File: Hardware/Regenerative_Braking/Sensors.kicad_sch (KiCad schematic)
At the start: 48 parts, among them IC4 LM339DT

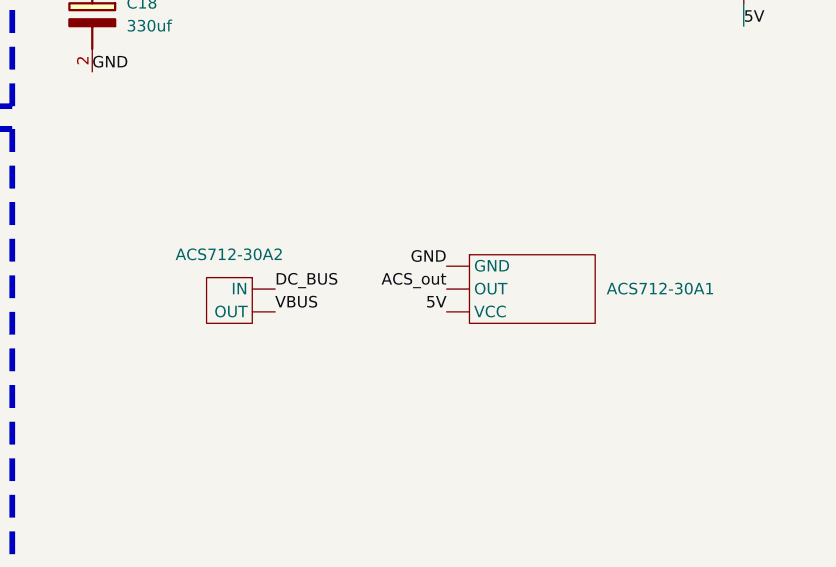
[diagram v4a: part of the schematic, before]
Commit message: Added Battery side
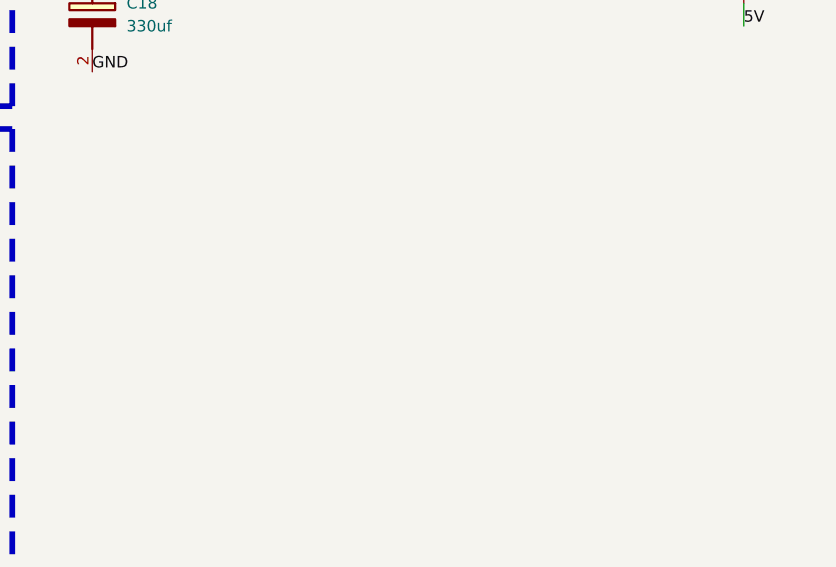
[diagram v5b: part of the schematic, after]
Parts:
- removed ACS712-30A1: (no value), Regen_braking:ACS712_Module_27x12mm, symbol Regen_braking:ACS712-30A
- removed ACS712-30A2: (no value), Regen_braking:Solderpad_acs712_INOUT, symbol Regen_braking:solder_pad_acs712_inout
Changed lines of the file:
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@@
 		)
 	)
-	(label "ACS_out"
-		(at 241.3 78.74 180)
-		(effects
-			(font
-				(size 1.27 1.27)
-			)
-			(justify right bottom)
-		)
-	)
 	(label "3V3"
 		(at 160.02 77.47 90)
@@
 	)
 	(label "VBUS"
-		(at 222.25 81.28 0)
-		(effects
-			(font
-				(size 1.27 1.27)
-			)
-			(justify left bottom)
-		)
-	)
-	(label "VBUS"
 		(at 27.94 161.29 180)
 		(effects
@@
 		)
 	)
-	(label "DC_BUS"
-		(at 222.25 78.74 0)
-		(effects
-			(font
-				(size 1.27 1.27)
-			)
-			(justify left bottom)
-		)
-	)
 	(label "3V3"
 		(at 81.28 102.87 0)
@@
 	)
 	(label "GND"
-		(at 241.3 76.2 180)
-		(effects
-			(font
-				(size 1.27 1.27)
-			)
-			(justify right bottom)
-		)
-	)
-	(label "GND"
 		(at 262.89 36.83 0)
 		(effects
@@
 		)
 	)
-	(label "5V"
-		(at 241.3 81.28 180)
-		(effects
-			(font
-				(size 1.27 1.27)
-			)
-			(justify right bottom)
-		)
-	)
 	(label "3V3"
 		(at 120.65 77.47 90)
@@
 	)
 	(symbol
-		(lib_id "Regen_braking:ACS712-30A")
-		(at 250.19 78.74 0)
-		(unit 1)
-		(body_style 1)
-		(exclude_from_sim no)
-		(in_bom yes)
-		(on_board yes)
-		(in_pos_files yes)
-		(dnp no)
-		(fields_autoplaced yes)
-		(property "Reference" "ACS712-30A1"
-			(at 259.08 78.74 0)
-			(show_name no)
-			(do_not_autoplace no)
-			(effects
-				(font
-					(size 1.27 1.27)
-				)
-				(justify left)
-			)
-		)
-		(property "Value" ""
-			(at 250.19 78.74 0)
-			(show_name no)
-			(do_not_autoplace no)
-			(effects
-				(font
-					(size 1.27 1.27)
-				)
-			)
-		)
-		(property "Footprint" "Regen_braking:ACS712_Module_27x12mm"
-			(at 250.19 78.74 0)
-			(hide yes)
-			(show_name no)
-			(do_not_autoplace no)
-			(effects
-				(font
-					(size 1.27 1.27)
-				)
-			)
-		)
-		(property "Datasheet" ""
-			(at 250.19 78.74 0)
-			(hide yes)
-			(show_name no)
-			(do_not_autoplace no)
-			(effects
-				(font
-					(size 1.27 1.27)
-				)
-			)
-		)
-		(property "Description" ""
-			(at 250.19 78.74 0)
-			(hide yes)
-			(show_name no)
-			(do_not_autoplace no)
-			(effects
-				(font
-					(size 1.27 1.27)
-				)
-			)
-		)
-		(pin ""
-		)
-		(pin ""
-		)
-		(pin ""
-		)
-		(instances
-			(project "Regenerative_Braking"
-				(path "/058fbdf2-a911-4044-912a-e4c9081c01f8/31ad71cf-e5d8-4161-a0e2-bbb3e789d0af"
-					(reference "ACS712-30A1")
-					(unit 1)
-				)
-			)
-		)
-	)
-	(symbol
 		(lib_id "Regen_braking:47,2.2,100k,10k,4.7,10ohm")
 		(at 140.97 35.56 0)
@@
 					(unit 1)
 				)
-			)
-		)
-	)
-	(symbol
-		(lib_id "Regen_braking:solder_pad_acs712_inout")
-		(at 217.17 83.82 0)
-		(unit 1)
-		(body_style 1)
-		(exclude_from_sim no)
-		(in_bom yes)
-		(on_board yes)
-		(in_pos_files yes)
-		(dnp no)
-		(fields_autoplaced yes)
-		(property "Reference" "ACS712-30A2"
-			(at 217.17 74.93 0)
-			(show_name no)
-			(do_not_autoplace no)
-			(effects
-				(font
-					(size 1.27 1.27)
-				)
-			)
-		)
-		(property "Value" ""
-			(at 217.17 83.82 0)
-			(show_name no)
-			(do_not_autoplace no)
-			(effects
-				(font
-					(size 1.27 1.27)
-				)
-			)
-		)
-		(property "Footprint" "Regen_braking:Solderpad_acs712_INOUT"
-			(at 217.17 83.82 0)
-			(hide yes)
-			(show_name no)
-			(do_not_autoplace no)
-			(effects
-				(font
-					(size 1.27 1.27)
-				)
-			)
-		)
-		(property "Datasheet" ""
-			(at 217.17 83.82 0)
-			(hide yes)
-			(show_name no)
-			(do_not_autoplace no)
-			(effects
-				(font
-					(size 1.27 1.27)
-				)
-			)
-		)
-		(property "Description" ""
-			(at 217.17 83.82 0)
-			(hide yes)
-			(show_name no)
-			(do_not_autoplace no)
-			(effects
-				(font
-					(size 1.27 1.27)
-				)
-			)
-		)
-		(pin ""
-		)
-		(pin ""
-		)
-		(instances
-			(project "Regenerative_Braking"
-				(path "/058fbdf2-a911-4044-912a-e4c9081c01f8/31ad71cf-e5d8-4161-a0e2-bbb3e789d0af"
-					(reference "ACS712-30A2")
-					(unit 1)
-				)

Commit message: finished everything except mcu
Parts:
- removed C18: 330uf, Regen_braking:330uf_25v_cap_5v_buck, symbol Regen_braking:330uf_25v_cap_5v_buck
- removed C24: 120uf, Regen_braking:120uf_cap_5v_buck, symbol Regen_braking:120uf_cap_5v_buck
- removed D10: 1N5822, Regen_braking:1N5822, symbol Regen_braking:1N5822
- removed L1: 47uH, Regen_braking:47uh_5v_buck, symbol Regen_braking:47uh_5v_buck
- removed VR1: LM2596S-5.0, Regen_braking:5v_buck, symbol Regen_braking:LM2596S-5.0
- added ACS712-30A1, ACS712-30A4: (no value), Regen_braking:ACS712_Module_27x12mm, symbol Regen_braking:ACS712-30A
- added ACS712-30A2, ACS712-30A3: (no value), Regen_braking:Solderpad_acs712_INOUT, symbol Regen_braking:solder_pad_acs712_inout
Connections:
- net 5V: now also ACS712-30A1. (VCC), ACS712-30A4. (VCC)
- net ACS_out: now also ACS712-30A1. (VCC)
- net GND: now also ACS712-30A1. (VCC), ACS712-30A4. (VCC)
- net VBUS: now also ACS712-30A2. (OUT)
- new net ACS_in: ACS712-30A3. (OUT)
- new net Cap_bufferBank: ACS712-30A3. (OUT)
- new net DC_BUS: ACS712-30A2. (OUT)
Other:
- note added: "CURRENT SENSING BLOCK"

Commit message: MCU CONNECTIONS
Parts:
- added J2: Conn_01x03, symbol Connector_Generic:Conn_01x03
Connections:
- net VSENSE_BAT: now reaches C10.1, D_OV4.1, D_UV4.2, R29.2
- net U_mid renamed U_ADC1
- net V_mid renamed V_ADC1
- net W_mid renamed W_ADC1
- new net HALL_U: J2.1 (Pin_1)
- new net HALL_V: J2.2 (Pin_2)
- new net HALL_W: J2.3 (Pin_3)
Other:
- note added: "HALL EFFECT SENSING"
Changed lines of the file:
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@@
 	(rectangle
 		(start 105.41 60.96)
-		(end 193.04 135.89)
+		(end 195.58 135.89)
 		(stroke
 			(width 0.635)
@@
 	)
 	(rectangle
+		(start 198.12 15.24)
+		(end 281.94 58.42)
+		(stroke
+			(width 0.635)
+			(type dash)
+			(color 0 0 255 1)
+		)
+		(fill
+			(type none)
+		)
+	)
+	(rectangle
 		(start 105.41 140.97)
 		(end 205.74 161.29)
@@
 	(rectangle
 		(start 105.41 15.24)
-		(end 193.04 58.42)
+		(end 195.58 58.42)
 		(stroke
 			(width 0.635)
@@
 		)
 	)
+	(text "HALL EFFECT SENSING\n"
+		(exclude_from_sim no)
+		(at 242.57 18.796 0)
+		(effects
+			(font
+				(size 2.54 2.54)
+			)
+		)
+	)
 	(junction
 		(at 170.18 35.56)
@@
 	(wire
 		(pts
+			(xy 243.84 29.21) (xy 246.38 29.21)
+		)
+		(stroke
+			(width 0)
+			(type default)
+		)
+	)
+	(wire
+		(pts
 			(xy 135.89 36.83) (xy 135.89 35.56)
 		)
@@
 	(wire
 		(pts
+			(xy 243.84 26.67) (xy 246.38 26.67)
+		)
+		(stroke
+			(width 0)
+			(type default)
+		)
+	)
+	(wire
+		(pts
 			(xy 81.28 35.56) (xy 93.98 35.56)
 		)
@@
 	(wire
 		(pts
+			(xy 243.84 31.75) (xy 246.38 31.75)
+		)
+		(stroke
+			(width 0)
+			(type default)
+		)
+	)
+	(wire
+		(pts
 			(xy 74.93 124.46) (xy 74.93 129.54)
 		)
@@
 		)
 	)
+	(label "W_ADC1"
+		(at 182.88 101.6 0)
+		(effects
+			(font
+				(size 1.27 1.27)
+			)
+			(justify left bottom)
+		)
+	)
 	(label "GND"
 		(at 40.64 181.61 0)
@@
 		)
 	)
+	(label "V_ADC1"
+		(at 111.76 104.14 180)
+		(effects
+			(font
+				(size 1.27 1.27)
+			)
+			(justify right bottom)
+		)
+	)
 	(label "3V3"
 		(at 120.65 69.85 90)
@@
 		)
 	)
-	(label "W_mid"
+	(label "W_ADC1"
 		(at 95.25 114.3 0)
 		(effects
@@
 		)
 	)
+	(label "U_ADC1"
+		(at 111.76 99.06 180)
+		(effects
+			(font
+				(size 1.27 1.27)
+			)
+			(justify right bottom)
+		)
+	)
 	(label "GND"
 		(at 46.99 134.62 0)
@@
 		)
 	)
-	(label "U_mid"
+	(label "HALL_U"
+		(at 243.84 26.67 180)
+		(effects
+			(font
+				(size 1.27 1.27)
+			)
+			(justify right bottom)
+		)
+	)
+	(label "U_ADC1"
 		(at 93.98 35.56 0)
 		(effects
@@
 		)
 	)
-	(label "V_mid"
-		(at 111.76 104.14 180)
+	(label "5V"
+		(at 186.69 154.94 180)
 		(effects
 			(font
@@
 		)
 	)
-	(label "5V"
-		(at 186.69 154.94 180)
+	(label "HALL_V"
+		(at 243.84 29.21 180)
 		(effects
 			(font
@@
 		)
 	)
+	(label "VSENSE_BAT"
+		(at 182.88 35.56 0)
+		(effects
+			(font
+				(size 1.27 1.27)
+			)
+			(justify left bottom)
+		)
+	)
 	(label "GND"
 		(at 81.28 129.54 0)
@@
 		)
 	)
-	(label "V_mid"
+	(label "V_ADC1"
 		(at 95.25 73.66 0)
 		(effects
@@
 		)
 	)
+	(label "HALL_W"
+		(at 243.84 31.75 180)
+		(effects
+			(font
+				(size 1.27 1.27)
+			)
+			(justify right bottom)
+		)
+	)
 	(label "3V3"
 		(at 120.65 77.47 90)
@@
 		)
 	)
-	(label "W_mid"
-		(at 182.88 101.6 0)
-		(effects
-			(font
-				(size 1.27 1.27)
-			)
-			(justify left bottom)
-		)
-	)
 	(label "OUT1"
 		(at 111.76 91.44 180)
@@
 		)
 	)
-	(label "U_mid"
-		(at 111.76 99.06 180)
-		(effects
-			(font
-				(size 1.27 1.27)
-			)
-			(justify right bottom)
-		)
-	)
 	(label "ACS_in"
 		(at 118.11 153.67 0)
@@
 	)
 	(symbol
+		(lib_id "Connector_Generic:Conn_01x03")
+		(at 251.46 29.21 0)
+		(unit 1)
+		(body_style 1)
+		(exclude_from_sim no)
+		(in_bom yes)
+		(on_board yes)
+		(in_pos_files yes)
+		(dnp no)
+		(fields_autoplaced yes)
+		(property "Reference" "J2"
+			(at 254 27.9399 0)
+			(show_name no)
+			(do_not_autoplace no)
+			(effects
+				(font
+					(size 1.27 1.27)
+				)
+				(justify left)
+			)
+		)
+		(property "Value" "Conn_01x03"
+			(at 254 30.4799 0)
+			(show_name no)
+			(do_not_autoplace no)
+			(effects
+				(font
+					(size 1.27 1.27)
+				)
+				(justify left)
+			)
+		)
+		(property "Footprint" ""
+			(at 251.46 29.21 0)
+			(hide yes)
+			(show_name no)
+			(do_not_autoplace no)
+			(effects
+				(font
+					(size 1.27 1.27)
+				)
+			)
+		)
+		(property "Datasheet" ""
+			(at 251.46 29.21 0)
+			(hide yes)
+			(show_name no)
+			(do_not_autoplace no)
+			(effects
+				(font
+					(size 1.27 1.27)
+				)
+			)
+		)
+		(property "Description" "Generic connector, single row, 01x03, script generated (kicad-library-utils/schlib/autogen/connector/)"
+			(at 251.46 29.21 0)
+			(hide yes)
+			(show_name no)
+			(do_not_autoplace no)
+			(effects
+				(font
+					(size 1.27 1.27)
+				)
+			)
+		)
+		(pin "3"
+		)
+		(pin "2"
+		)
+		(pin "1"
+		)
+		(instances
+			(project "Regenerative_Braking"
+				(path "/058fbdf2-a911-4044-912a-e4c9081c01f8/31ad71cf-e5d8-4161-a0e2-bbb3e789d0af"
+					(reference "J2")
+					(unit 1)
+				)
+			)
+		)
+	)
+	(symbol
 		(lib_id "Regen_braking:100nf_rcFilter")
 		(at 74.93 40.64 90)
@@
 		(in_pos_files yes)
 		(dnp no)
-		(fields_autoplaced yes)
 		(property "Reference" "R22"
 			(at 123.19 124.46 0)
@@
 		)
 		(property "Value" "2.2k"
-			(at 123.19 127 0)
+			(at 114.554 125.73 0)
 			(show_name no)
 			(do_not_autoplace no)
@@
 		)
 		(property "Value" "100nf_rcFilter"
-			(at 138.43 127 90)
+			(at 140.97 126.492 90)
 			(show_name no)
 			(do_not_autoplace no)

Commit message: finished schematic
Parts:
- removed C10: 100nf_rcFilter, Regen_braking:100nf_rcFilter, symbol Regen_braking:100nf_rcFilter
- removed D_OV4, D_OV6, D_UV4, D_UV6: BAT54T1G, Regen_braking:BAT54T1G, symbol Regen_braking:BAT54T1G
- removed R19: 1k, Regen_braking:47,2.2,100k,10k,4.7,10ohm, symbol Device:R
- added C36, C37, C38: 10nf_rcFilter, Capacitor_SMD:C_1206_3216Metric, symbol Regen_braking:100nf_rcFilter
- added C40, C41: 100nf_rcFilter, Capacitor_SMD:C_1206_3216Metric, symbol Regen_braking:100nf_rcFilter
- added D_OV10, D_OV8, D_OV9, D_UV10, D_UV8, D_UV9: BAT54T1G, Regen_braking:SODFL3718X115, symbol Regen_braking:BAT54T1G
- added R19, R30, R31, R33: 10k, Resistor_THT:R_Axial_DIN0204_L3.6mm_D1.6mm_P7.62mm_Horizontal, symbol Regen_braking:47,2.2,100k,10k,4.7,10ohm
- added R32: 100k, Resistor_THT:R_Axial_DIN0207_L6.3mm_D2.5mm_P7.62mm_Horizontal, symbol Regen_braking:47,2.2,100k,10k,4.7,10ohm
- added R34, R36: 4.7k, Resistor_THT:R_Axial_DIN0204_L3.6mm_D1.6mm_P7.62mm_Horizontal, symbol Regen_braking:47,2.2,100k,10k,4.7,10ohm
- added R40, R41, R42, R43: 1k, Resistor_THT:R_Axial_DIN0204_L3.6mm_D1.6mm_P7.62mm_Horizontal, symbol Regen_braking:47,2.2,100k,10k,4.7,10ohm
- ACS712-30A2, ACS712-30A3: footprint Regen_braking:Solderpad_acs712_INOUT -> Regen_braking:ACS_pad
- C17, C20, C7, C8, C9: footprint Regen_braking:100nf_rcFilter -> Capacitor_SMD:C_1206_3216Metric
- C19: value 100nf -> 100nf_rcFilter; footprint C1206C104J5RACTU:CAPC3216X88N -> Capacitor_SMD:C_1206_3216Metric
- D_OV1, D_OV2, D_OV3, D_OV5, D_UV1, D_UV2, D_UV3, D_UV5: footprint Regen_braking:BAT54T1G -> Regen_braking:SODFL3718X115
- IC4: footprint Regen_braking:LM339DT -> Regen_braking:SOIC127P600X175-14N
- J2: footprint (none) -> Regen_braking:Hall_UVW
- R1, R2, R22, R3, R7: footprint Regen_braking:47,2.2,100k,10k,4.7,10ohm -> Resistor_THT:R_Axial_DIN0207_L6.3mm_D2.5mm_P7.62mm_Horizontal
- R15: footprint Regen_braking:220kohm_divider -> Resistor_THT:R_Axial_DIN0207_L6.3mm_D2.5mm_P10.16mm_Horizontal
- R16, R17, R18, R20, R21, R25, R26, R27, R28, R29, R4, R5, R6, R8: footprint Regen_braking:47,2.2,100k,10k,4.7,10ohm -> Resistor_THT:R_Axial_DIN0204_L3.6mm_D1.6mm_P7.62mm_Horizontal
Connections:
- net 3V3: now also R17.2, R18.2, R20.2, R21.2, D_OV10.2, D_OV8.2, D_OV9.2, R19.2, R30.2, R31.2; no longer R17.1, R18.1, R20.1, R21.1
- net 5V: now also C20.1, R40.1; no longer C19.1
- net Cap_bufferBank: now also R32.1
- net GND: now also C36.2, C37.2, C38.2, C40.2, C41.2, D_UV10.1, D_UV8.1, D_UV9.1, R33.2
- net OC_mid: now also C19.1, D_OV9.1, D_UV9.2, R36.2; no longer C20.1
- net OUT1: now also R20.1; no longer R17.2
- net OUT2: now also R17.1; no longer R18.2
- net OUT3: now also R21.1; no longer R21.2
- net OUT4: now also R18.1; no longer R20.2
- net VSENSE_BAT: now also C40.1, D_OV8.1, D_UV8.2
- net at R22.2: now also R36.1, R40.2
- net ACS_out renamed ACS1
- net HALL_U renamed HU
- net HU: now also R19.1, R41.2
- net HALL_V renamed HV
- net HV: now also R30.1, R42.2
- net HALL_W renamed HW
- net HW: now also R31.1, R43.2
- new net: R32.2, R33.1, R34.1
- new net ACS2: ACS712-30A4. (VCC)
- new net Hall_U: C36.1, R41.1
- new net Hall_V: C37.1, R42.1
- new net Hall_W: C38.1, R43.1
- new net VSENSE_CAP: C41.1, D_OV10.1, D_UV10.2, R34.2
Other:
- note added: "CAP BANK VOLTAGE SENSING"
- moved on the sheet: ACS712-30A1, ACS712-30A2, ACS712-30A4, J2, R22
